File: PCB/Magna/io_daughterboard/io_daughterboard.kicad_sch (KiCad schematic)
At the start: 7 parts, among them J101 Conn_02x10_Counter_Clockwise

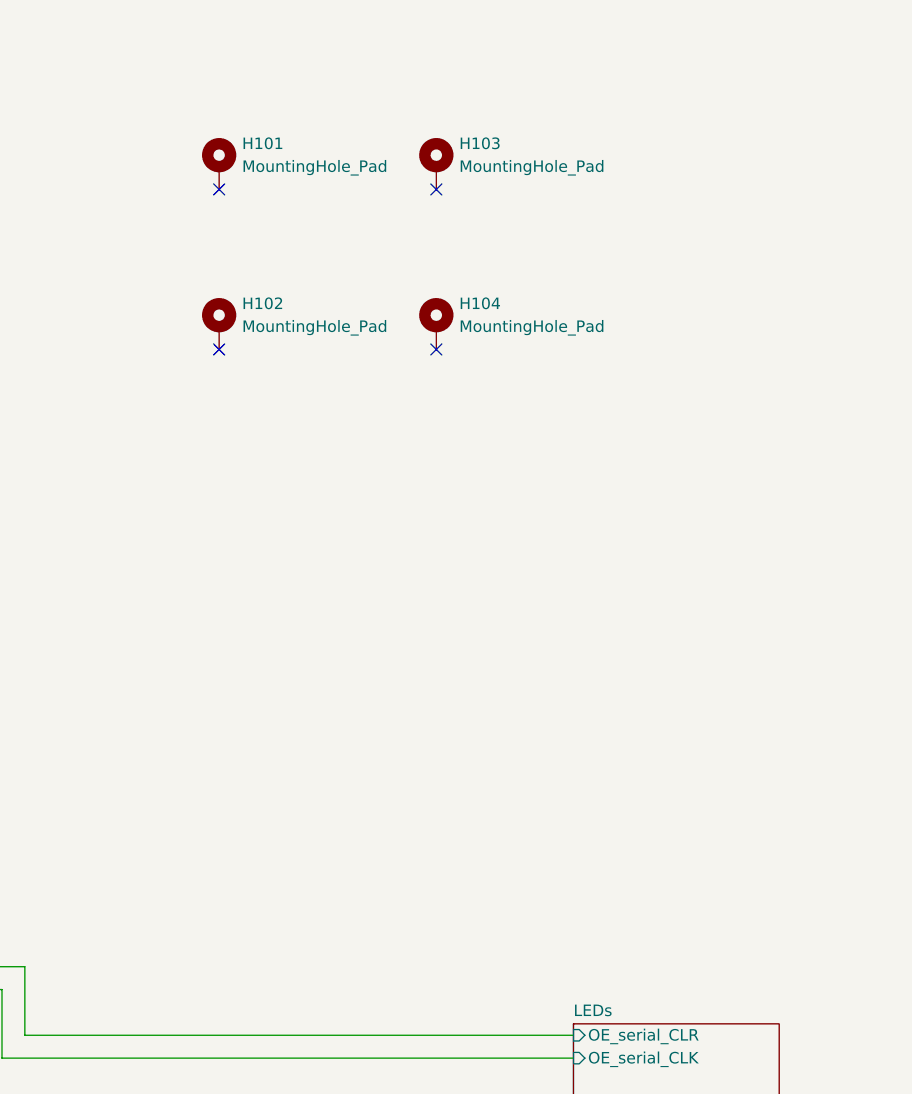
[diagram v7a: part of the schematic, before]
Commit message: Fix some more small issues on IO board
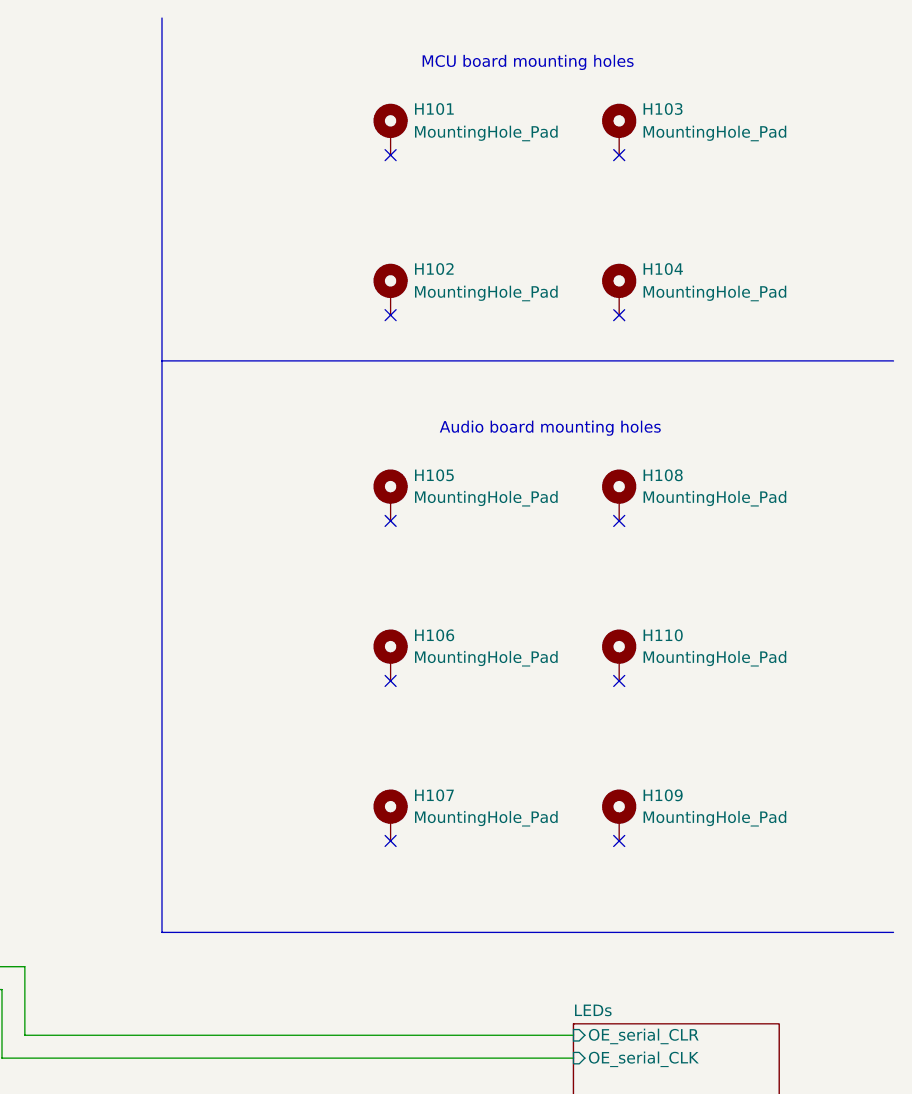
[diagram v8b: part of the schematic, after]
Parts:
- added H105, H106, H107, H108, H109, H110: MountingHole_Pad, MountingHole:MountingHole_3.2mm_M3_Pad_Via, symbol Mechanical:MountingHole_Pad
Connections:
- no-connect marks 4 -> 10
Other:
- note added: "Audio board mounting holes"
- note added: "MCU board mounting holes"
- moved on the sheet: H101, H102, H103, H104
